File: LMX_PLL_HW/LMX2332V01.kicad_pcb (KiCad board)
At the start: 2 copper layers, 42 parts, among them U1 Z-CommV440, U2 LMX2332, U4 TPS784-Q1, U5 TPS784-Q1

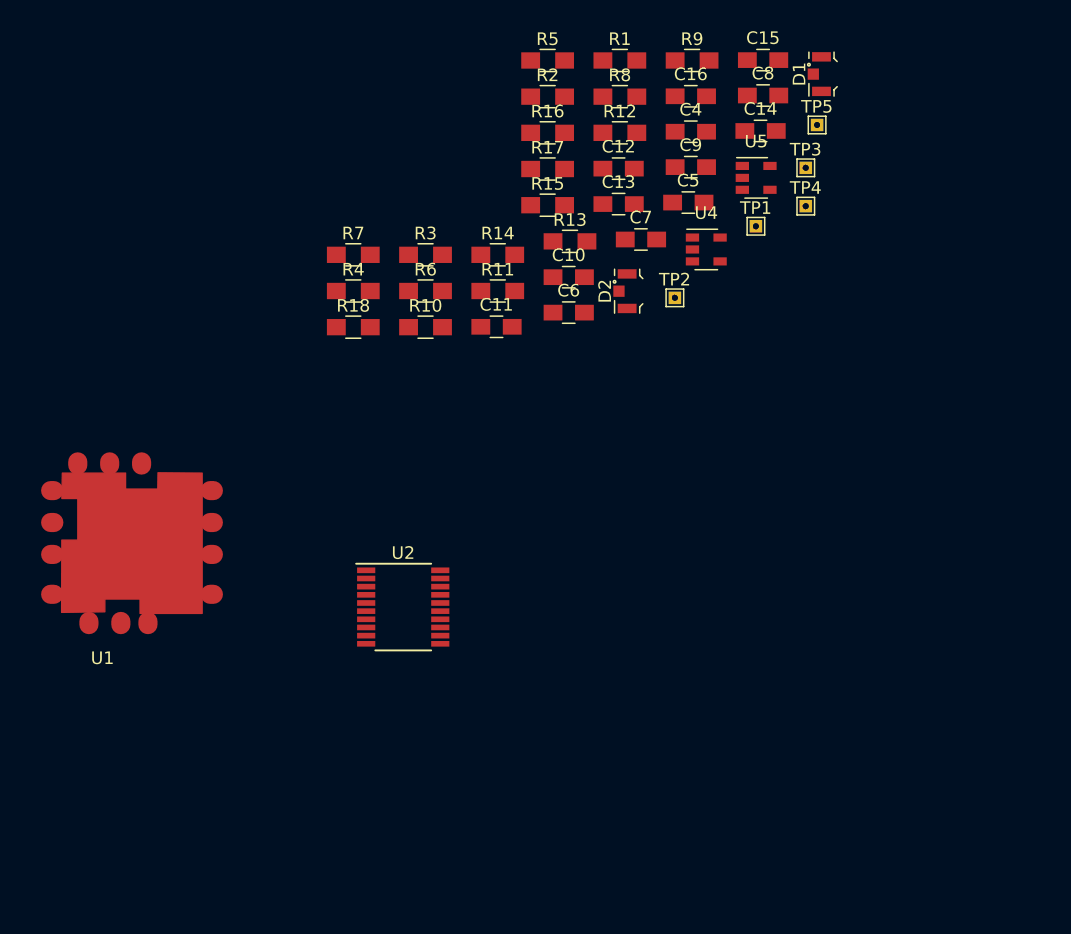
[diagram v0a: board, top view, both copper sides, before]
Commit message: Update 2021-07-05
Finished Schematic enough to get a first cut pulled into the layout.

Also finished PLL_Calculations.py enought to get loop filter component footprints nailed. Still needs more work, but ongoing. I'm using Spyder as a Python IDE.
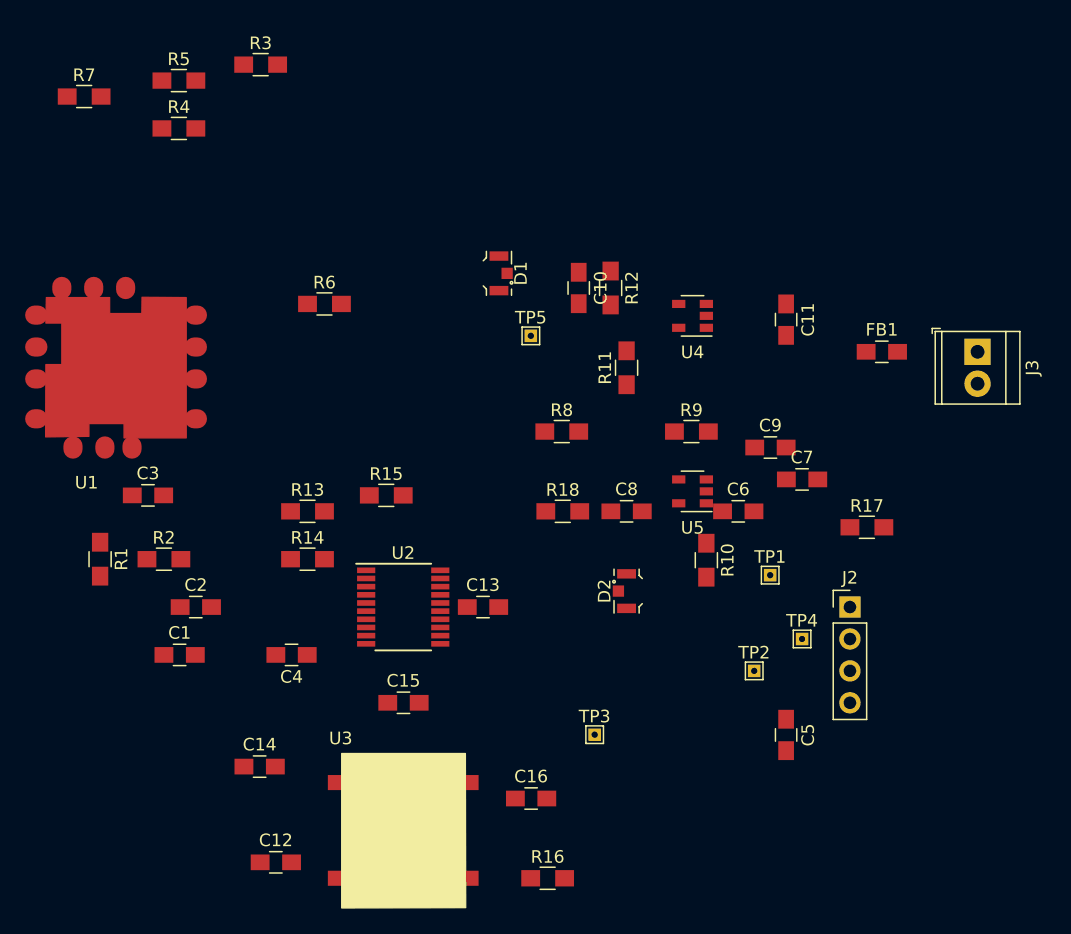
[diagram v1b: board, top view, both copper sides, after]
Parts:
- added C1: 120pF, Capacitors_SMD:C_0805_HandSoldering, F.Cu at (110.5, 95.2)
- added C2: 820pF, Capacitors_SMD:C_0805_HandSoldering, F.Cu at (111.8, 91.4)
- added C3: DNP, Capacitors_SMD:C_0805_HandSoldering, F.Cu at (108.0, 82.5)
- added FB1: Ferrite_Bead_Small, Capacitors_SMD:C_0805_HandSoldering, F.Cu at (166.4, 71.1)
- added J2: Conn_01x04_Male, Connector_PinHeader_2.54mm:PinHeader_1x04_P2.54mm_Vertical, F.Cu at (163.8, 91.4)
- added J3: Screw_Terminal_01x02, TerminalBlock_TE-Connectivity:TerminalBlock_TE_282834-2_1x02_P2.54mm_Horizontal, F.Cu at (174.0, 71.1)
- added U3: ToyocomTCXO, LMX_PLL_HW:ToyocomTCXO, F.Cu at (128.3, 109.2)
- R1: value R_US -> 0
- R2: value R_US -> 53k6
- moved C14 64.4 mm to (116.8, 104.1)
- moved C12 61.6 mm to (118.1, 111.8)
- moved R16 59.3 mm to (139.8, 113.0)
- moved C15 58.6 mm to (128.3, 99.1)
- moved R1 57.3 mm to (104.1, 87.6), turned to 270 degrees
- moved C16 57.3 mm to (138.4, 106.7)
- moved C4 52.4 mm to (119.4, 95.2), turned to 180 degrees
- moved TP3 48.2 mm to (143.5, 101.6)
- moved R2 47.8 mm to (109.2, 87.6)
- moved C5 43.1 mm to (158.8, 101.6), turned to 270 degrees
- moved R17 38.2 mm to (165.2, 85.1)
- moved C8 34.8 mm to (146.1, 83.8)
- moved TP4 34.5 mm to (160.0, 94.0)
- moved C13 33.8 mm to (134.6, 91.4)
- moved TP2 30.4 mm to (156.2, 96.5)
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
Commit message: Layout Updates
Almost OK.
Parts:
- moved R7 53.1 mm to (138.4, 90.2)
- moved R17 40.4 mm to (135.9, 57.2), turned to 90 degrees
- moved R6 30.2 mm to (138.3, 92.7)
- moved C12 28.1 mm to (127.0, 85.1), turned to 90 degrees
- moved C7 27.9 mm to (141.0, 61.0), turned to 90 degrees
- moved C6 24.4 mm to (143.5, 62.2), turned to 90 degrees
- moved TP5 23.9 mm to (148.6, 91.4)
- moved J3 22.6 mm to (156.2, 85.1)
- moved FB1 21.6 mm to (149.9, 85.1)
- moved C14 20.5 mm to (124.5, 85.1), turned to 90 degrees
- moved R16 19.9 mm to (127.0, 97.8)
- moved C5 19.9 mm to (146.1, 86.4)
- moved D2 19.5 mm to (135.9, 73.6)
- moved C16 18.3 mm to (123.2, 96.5), turned to 270 degrees
- moved R3 18.2 mm to (113.0, 66.0), turned to 270 degrees
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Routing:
- net Net-(J2-Pad3): track 0.00 -> 30.8 mm
- net Net-(J2-Pad2): track 0.00 -> 29.3 mm
- net Net-(J2-Pad1): track 0.00 -> 28.2 mm
- net +5V: track 0.00 -> 22.0 mm
- net Net-(C1-Pad1): track 0.00 -> 21.2 mm
- net Net-(C3-Pad1): track 0.00 -> 9.28 mm
- net Net-(TP3-Pad1): track 0.00 -> 8.18 mm
- net Net-(C16-Pad2): track 0.00 -> 7.00 mm
- net Net-(R8-Pad1): track 0.00 -> 6.69 mm
- net Net-(R7-Pad1): track 0.00 -> 6.25 mm
- net Net-(R6-Pad1): track 0.00 -> 6.17 mm
- net Net-(C4-Pad1): track 0.00 -> 5.07 mm
- net Net-(C16-Pad1): track 0.00 -> 3.78 mm
- net Net-(C2-Pad1): track 0.00 -> 2.47 mm
- added copper zone on B.Cu, net GND
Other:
- board outline added: 59.7 x 59.7 mm

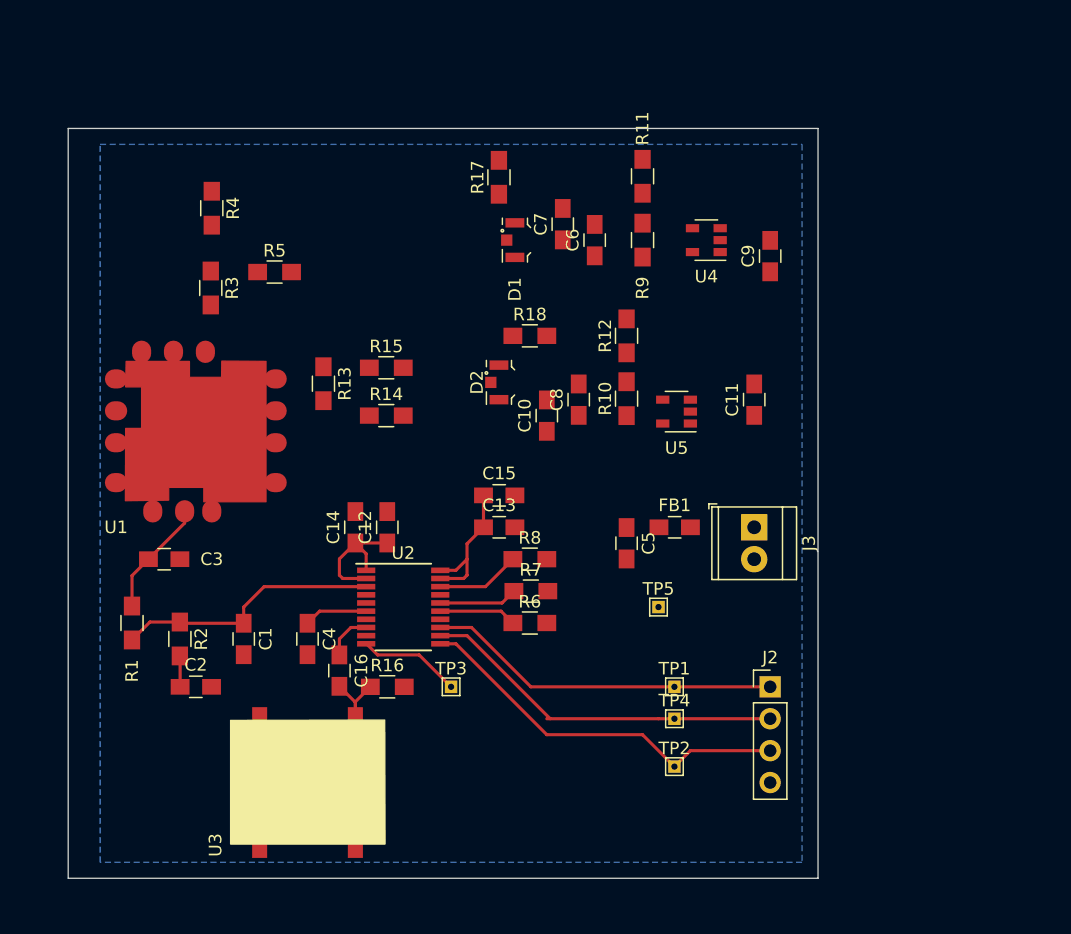
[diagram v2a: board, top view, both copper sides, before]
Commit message: PCB Layout Updates. Not completed yet
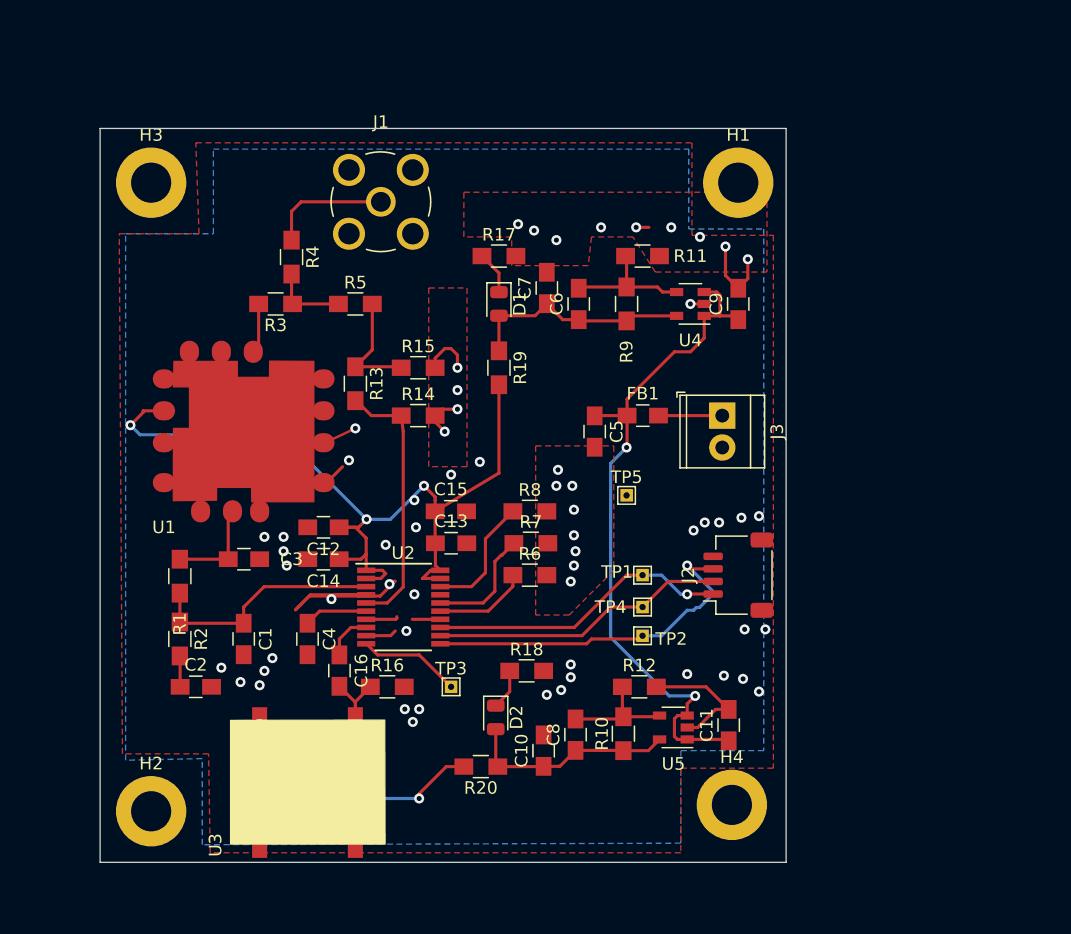
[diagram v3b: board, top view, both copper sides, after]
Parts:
- added H1: MountingHole, Mounting_Holes:MountingHole_3.2mm_M3_DIN965_Pad, F.Cu at (154.9, 57.7)
- added H2: MountingHole, Mounting_Holes:MountingHole_3.2mm_M3_DIN965_Pad, F.Cu at (108.2, 107.7)
- added H3: MountingHole, Mounting_Holes:MountingHole_3.2mm_M3_DIN965_Pad, F.Cu at (108.2, 57.7)
- added H4: MountingHole, Mounting_Holes:MountingHole_3.2mm_M3_DIN965_Pad, F.Cu at (154.4, 107.2)
- added J1: 142-0701-201, LMX_PLL_HW:JOHNSON_142-0701-201, F.Cu at (126.5, 59.2)
- added R19: 0, Resistors_SMD:R_0805_HandSoldering, F.Cu at (135.9, 72.4)
- added R20: 0, Resistors_SMD:R_0805_HandSoldering, F.Cu at (134.4, 104.1)
- D1, D2: footprint LED_SMD:LED_LiteOn_LTST-S326 -> LED_SMD:LED_0805_2012Metric
- J2: footprint Connector_PinHeader_2.54mm:PinHeader_1x04_P2.54mm_Vertical -> Connector_JST:JST_SH_SM04B-SRSS-TB_1x04-1MP_P1.00mm_Horizontal
- moved R12 28.0 mm to (147.1, 97.8), turned to 0 degrees
- moved C10 26.7 mm to (139.4, 102.9)
- moved R10 26.7 mm to (145.8, 101.5)
- moved R18 26.7 mm to (138.1, 96.5)
- moved C8 26.7 mm to (142.0, 101.6)
- moved D2 26.7 mm to (135.6, 100.2), turned to -90 degrees
- moved C11 26.0 mm to (154.2, 100.8)
- moved U5 25.1 mm to (149.8, 101.0)
- moved TP2 10.7 mm to (147.3, 93.7)
- moved C5 9.25 mm to (143.5, 77.5)
- moved J3 9.25 mm to (153.7, 76.2)
- moved TP1 9.25 mm to (147.3, 88.9)
- moved TP4 9.25 mm to (147.3, 91.4)
- moved FB1 9.25 mm to (147.3, 76.2)
- moved J2 9.25 mm to (154.9, 88.9), turned to 90 degrees
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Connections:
- C10 pad 1: +3V0 -> Net-(C10-Pad1)
- C6 pad 1: +5V -> Net-(C6-Pad1)
- C7 pad 1: +5V -> Net-(C6-Pad1)
- C8 pad 1: +3V0 -> Net-(C10-Pad1)
- D1 pad 2: +5V -> Net-(C6-Pad1)
- D2 pad 2: +3V0 -> Net-(C10-Pad1)
- R10 pad 1: +3V0 -> Net-(C10-Pad1)
- R9 pad 1: +5V -> Net-(C6-Pad1)
- U3 pad 5: Net-(U3-Pad5) -> unconnected-(U3-Pad5)
- U4 pad 5: +5V -> Net-(C6-Pad1)
- U5 pad 5: +3V0 -> Net-(C10-Pad1)
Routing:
- net VCC: track 0.00 -> 55.3 mm, vias 0 -> 2
- net GND: track 0.00 -> 53.0 mm, vias 0 -> 58
- net +5V: track 22.0 -> 67.3 mm, vias 0 -> 3
- net Net-(R13-Pad2): track 0.00 -> 21.3 mm
- net +3V0: track 0.00 -> 20.0 mm, vias 0 -> 3
- net Net-(C6-Pad1): track 0.00 -> 18.1 mm
- net Net-(C10-Pad1): track 0.00 -> 16.9 mm
- net Net-(C6-Pad2): track 0.00 -> 10.5 mm
- net Net-(J1-Pad1): track 0.00 -> 9.71 mm
- net Net-(R13-Pad1): track 0.00 -> 9.24 mm
- net Net-(C8-Pad2): track 0.00 -> 9.22 mm
- net Net-(R3-Pad1): track 0.00 -> 6.06 mm
- net Net-(J2-Pad2): track 29.3 -> 23.5 mm
- net Net-(FB1-Pad2): track 0.00 -> 5.08 mm
- net Net-(J2-Pad1): track 28.2 -> 24.1 mm, vias 0 -> 1
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- added copper zone on F.Cu, net GND
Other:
- board size 59.7 x 59.7 mm -> 54.6 x 58.4 mm
- net class Default removed

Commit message: As sent out to OshPark. Using KiCad 6.0.
As sent out to OshPark. Using KiCad 6.0.
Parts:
- removed TP1, TP2, TP3, TP4, TP5: TestPoint, TestPoint:TestPoint_THTPad_1.0x1.0mm_Drill0.5mm
- added 3V0: TestPoint, TestPoint:TestPoint_THTPad_D2.0mm_Drill1.0mm, F.Cu at (134.9, 110.0)
- added 5V0: TestPoint, TestPoint:TestPoint_THTPad_D2.0mm_Drill1.0mm, F.Cu at (140.0, 72.1)
- added CLK1: TestPoint, TestPoint:TestPoint_THTPad_D2.0mm_Drill1.0mm, F.Cu at (145.8, 92.7)
- added D3: TestPoint, TestPoint:TestPoint_THTPad_D2.0mm_Drill1.0mm, F.Cu at (145.8, 89.4)
- added FoLD1: TestPoint, TestPoint:TestPoint_THTPad_D2.0mm_Drill1.0mm, F.Cu at (132.1, 97.8)
- added GND1: TestPoint, TestPoint:TestPoint_THTPad_D2.0mm_Drill1.0mm, F.Cu at (139.2, 79.0)
- added LE1: TestPoint, TestPoint:TestPoint_THTPad_D2.0mm_Drill1.0mm, F.Cu at (145.8, 86.4)
- added VCont1: TestPoint, TestPoint:TestPoint_THTPad_D2.0mm_Drill1.0mm, F.Cu at (130.6, 110.0)
- C1: footprint Capacitors_SMD:C_0805_HandSoldering -> Capacitor_SMD:C_0805_2012Metric_Pad1.15x1.40mm_HandSolder
- J2: value Conn_01x04_Male -> Serial I/O; footprint Connector_JST:JST_SH_SM04B-SRSS-TB_1x04-1MP_P1.00mm_Horizontal -> Connector_JST:JST_PH_B4B-PH-K_1x04_P2.00mm_Vertical
- U1: value Z-CommV440 -> Z-CommV440V2; footprint LMX_PLL_HW:Z-CommVCO -> LMX_PLL_HW:ZCommVCO
- moved R18 10.2 mm to (138.3, 106.8)
- moved D2 6.82 mm to (133.7, 106.8), turned to 180 degrees
- moved J2 4.44 mm to (153.9, 84.6), turned to -90 degrees
- moved R12 3.87 mm to (143.3, 97.1)
- moved U5 3.86 mm to (146.0, 100.4)
- moved C10 3.81 mm to (135.6, 102.7)
- moved R20 3.81 mm to (130.6, 104.0)
- moved C8 3.81 mm to (138.2, 101.4)
- moved R10 3.81 mm to (142.0, 101.3)
- moved C11 2.53 mm to (151.7, 100.6), turned to 0 degrees
- moved R1 1.76 mm to (112.2, 89.0)
- moved R2 1.76 mm to (112.2, 94.0)
- moved C2 1.76 mm to (113.5, 97.8)
- moved H1 0.72 mm to (154.4, 57.1)
- moved H3 0.57 mm to (108.0, 57.1)
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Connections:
- net +5V renamed Net-(C12-Pad1)
- net VCC renamed Net-(C11-Pad1)
- J2 pad 1: Net-(J2-Pad1) -> GND
- J2 pad 2: Net-(J2-Pad2) -> Net-(CLK1-Pad1)
- J2 pad 3: Net-(J2-Pad3) -> Net-(D3-Pad1)
- J2 pad 4: GND -> Net-(J2-Pad4)
- U1 pad 4: (no net) -> GND
- U2 pad 11: Net-(J2-Pad3) -> Net-(CLK1-Pad1)
- U2 pad 12: Net-(J2-Pad2) -> Net-(D3-Pad1)
- U2 pad 13: Net-(J2-Pad1) -> Net-(J2-Pad4)
- U3 pad 5: unconnected-(U3-Pad5) -> Net-(U3-Pad5)
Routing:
- net Net-(C12-Pad1): track 67.3 -> 105.2 mm
- net Net-(J2-Pad4): track 0.00 -> 32.8 mm
- net Net-(J2-Pad3): track 28.9 -> 0.00 mm, vias 1 -> 0
- net GND: track 53.0 -> 26.0 mm, vias 58 -> 279
- net Net-(D3-Pad1): track 0.00 -> 25.2 mm
- net Net-(CLK1-Pad1): track 0.00 -> 25.0 mm
- net Net-(J2-Pad1): track 24.1 -> 0.00 mm, vias 1 -> 0
- net Net-(J2-Pad2): track 23.5 -> 0.00 mm
- net Net-(3V0-Pad1): track 16.9 -> 25.1 mm
- net +3V0: track 20.0 -> 13.8 mm, vias 3 -> 0
- net Net-(U3-Pad5): track 0.00 -> 6.02 mm
- net Net-(5V0-Pad1): track 18.1 -> 21.9 mm
- net (no net): track 2.17 -> 0.00 mm, vias 2 -> 0
- net Net-(C1-Pad1): track 19.1 -> 17.2 mm
- net Net-(C3-Pad1): track 7.80 -> 6.04 mm
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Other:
- outline, holes or cut-outs redrawn
- rule pad_to_mask_clearance: 0 -> 0.0508
- board text added: "1"
- board text added: "4"
- board text added: "LMX2332 V01"
- board text added: "\( ﾟヮﾟ)/"
